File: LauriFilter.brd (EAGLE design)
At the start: 39.3 x 106.5 mm, 27 parts, among them K1 MODE 1, K2 MODE 2

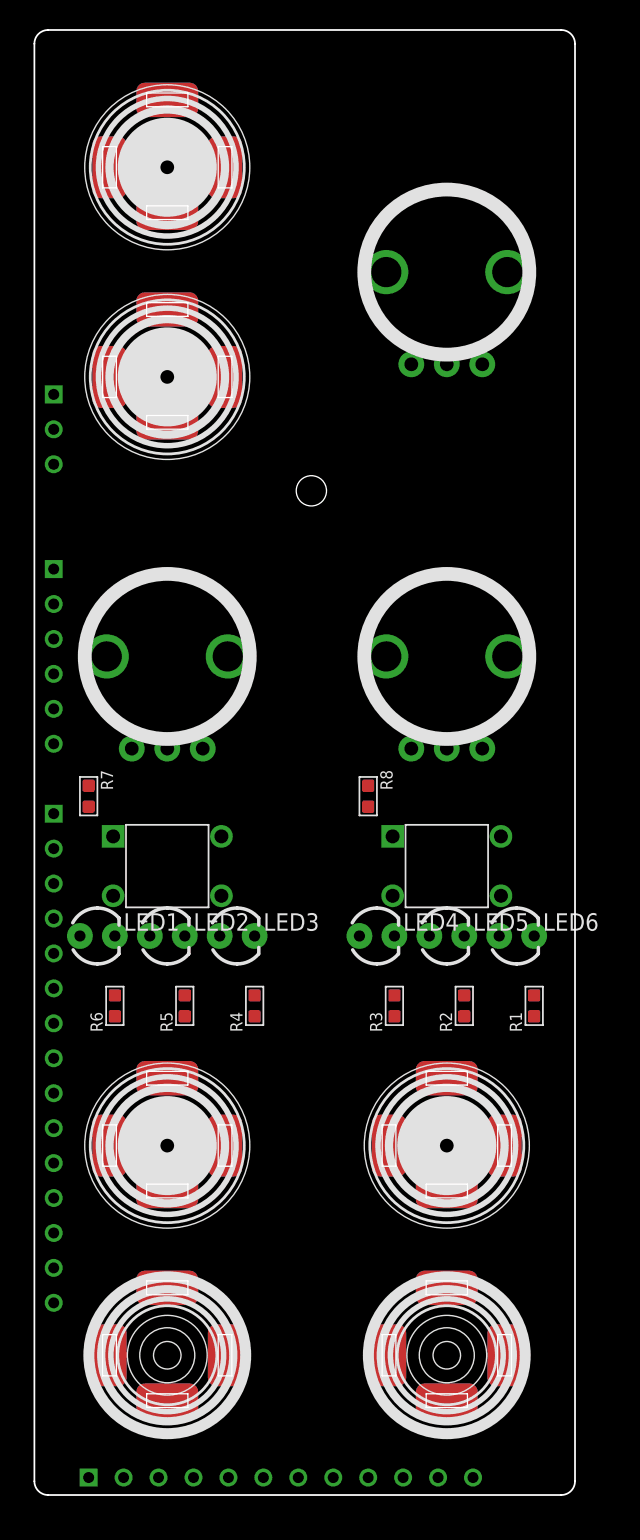
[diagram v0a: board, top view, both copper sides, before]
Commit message: LauriFilter has switches + 595 for leds
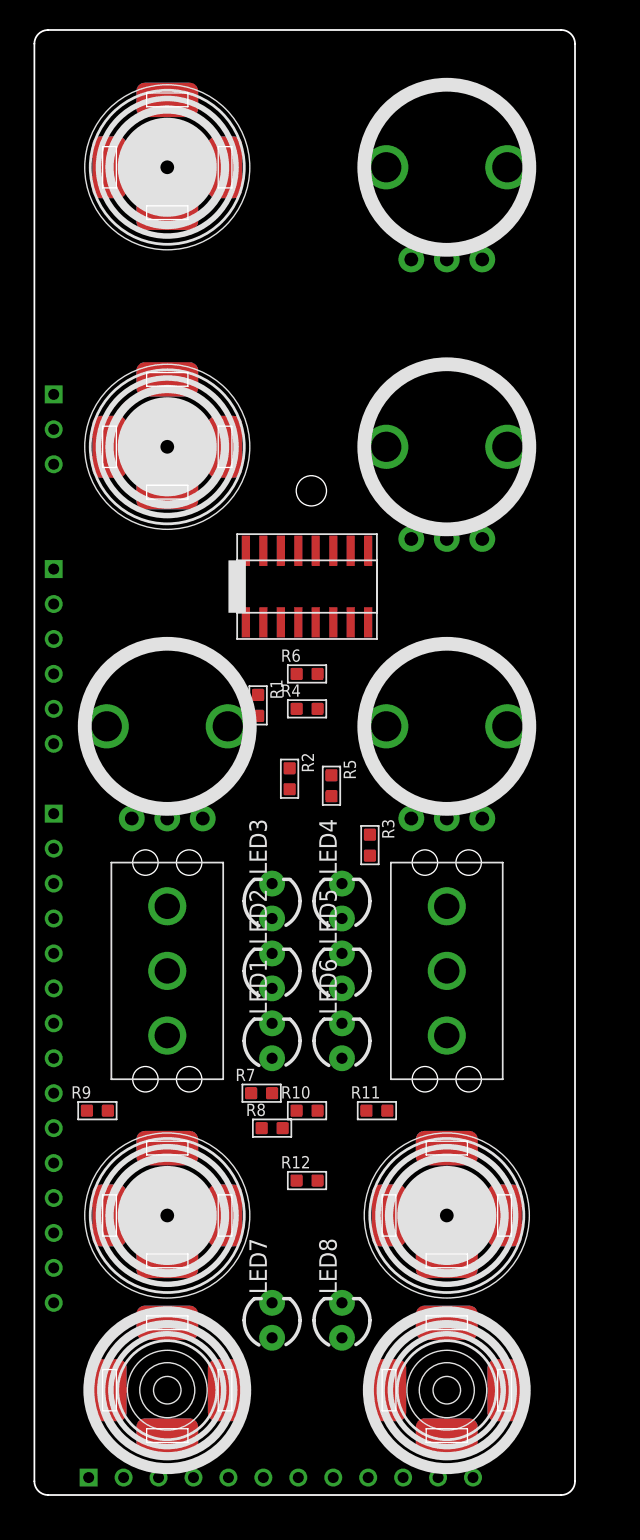
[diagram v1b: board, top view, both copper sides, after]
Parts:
- removed K1: MODE 1, OPL:4P-6.0X6.0X5.0H
- removed K2: MODE 2, OPL:4P-6.0X6.0X5.0H
- added IC2: IC_74HC595-SOIC-16, dp_devices:SOIC-16
- added LED7, LED8: (no value), SparkFun-LED:LED3MM
- added R10, R11, R12, R9: (no value), OPL:R0603
- added U$12, U$13: ONOFFON, EurorackModularParts:MULTICOMP1MS-ONOFFON
- added U$14: CV 2, EurorackModularParts:OG-POTS_ALPS_POT_VERTICAL
- moved R1 29.7 mm to (16.8, 57.4), turned to 270 degrees
- moved R6 27.9 mm to (20.3, 59.7), turned to 0 degrees
- moved R8 25.1 mm to (17.8, 26.7), turned to 0 degrees
- moved R7 25.0 mm to (17.0, 29.2), turned to 0 degrees
- moved R4 21.9 mm to (20.3, 57.1), turned to 0 degrees
- moved R2 20.8 mm to (19.1, 52.1), turned to 270 degrees
- moved R5 19.2 mm to (22.1, 51.6), turned to 270 degrees
- moved LED6 14.8 mm to (22.9, 33.0), turned to 90 degrees
- moved LED1 14.8 mm to (17.8, 33.0), turned to 90 degrees
- moved R3 11.8 mm to (24.9, 47.2), turned to 270 degrees
- moved LED2 8.03 mm to (17.8, 38.1), turned to 90 degrees
- moved LED5 8.03 mm to (22.9, 38.1), turned to 90 degrees
- moved U$9 7.62 mm to (30.5, 96.5)
- moved U$10 5.08 mm to (10.2, 55.9)
- moved U$11 5.08 mm to (30.5, 55.9)
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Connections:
- removed net MODE1: K1.1, K1.2, R7.2, U$1.ADC13
- removed net MODE2: K2.1, K2.2, R8.2, U$1.RX/B16
- removed net N$10: LED3.A, U$1.TX/D7
- removed net N$11: LED4.A, U$1.ADC4
- removed net N$12: LED5.A, U$1.ADC14
- new net LEDB1: IC2.15
- new net LEDB2: IC2.1
- new net LEDB3: IC2.2
- new net LEDB4: IC2.3
- new net LEDB5: IC2.4
- new net LEDB6: IC2.5
- new net LEDB7: IC2.6
- new net LEDB8: IC2.7
- new net LEDCLOCK: IC2.11, U$1.TX/D7
- new net LEDDAT: IC2.14, U$1.ADC4
- new net LEDLATCH: IC2.12, U$1.ADC7
- new net MODE1_A: R7.2, U$1.ADC13, U$12.1
- new net MODE1_B: R8.2, U$1.RX/B16, U$12.3
- new net MODE2_A: R9.2, U$1.TX/B17, U$13.1
- new net MODE2_B: R10.2, U$1.ADC14, U$13.3
- new net N$7: U$14.P$3, U$4.TIP@1, U$4.TIP@2
- net 3.3V: now also IC2.10, R10.1, R9.1
- net GND: now also IC2.13, LED1.A, LED2.A, LED3.A, LED4.A, LED5.A, LED6.A, LED7.A, LED8.A, U$12.2, U$13.2, U$14.P$1; no longer K1.3, K1.4, K2.3, K2.4, R1.1, R2.1, R3.1, R4.1, R5.1, R6.1
- net N$13: now also U$1.ADC6; no longer LED6.A, U$1.TX/B17
- net N$4: no longer U$4.TIP@1, U$4.TIP@2
- net N$8: now also LED8.K, R11.2; no longer LED1.A, U$1.ADC6
- net N$9: now also LED7.K, R12.2; no longer LED2.A, U$1.ADC7

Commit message: Preliminary routing LauriFilter
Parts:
- added C1: 100nF, OPL:C0603
- LED1, LED2, LED3, LED4, LED5, LED6, LED7, LED8: value (none) -> WHITE
- R1, R11, R12, R2, R3, R4, R5, R6: value (none) -> 50
- R10, R7, R8, R9: value (none) -> 10k
- moved IC2 41.9 mm to (20.3, 24.1), flipped to the bottom, turned to 270 degrees
- moved R6 28.0 mm to (14.0, 32.4), flipped to the bottom, turned to 90 degrees
- moved R1 26.9 mm to (26.7, 32.4), flipped to the bottom, turned to 90 degrees
- moved R8 22.5 mm to (33.7, 42.5), flipped to the bottom, turned to 90 degrees
- moved R10 19.8 mm to (6.99, 42.5), flipped to the bottom, turned to 90 degrees
- moved R7 17.2 mm to (33.7, 33.7), flipped to the bottom, turned to 270 degrees
- moved R2 16.5 mm to (26.7, 37.5), flipped to the bottom, turned to 90 degrees
- moved R5 16.3 mm to (14.0, 37.5), flipped to the bottom, turned to 90 degrees
- moved R4 15.9 mm to (14.0, 42.5), flipped to the bottom, turned to 90 degrees
- moved R11 11.1 mm to (22.9, 17.1), flipped to the bottom, turned to 270 degrees
- moved R12 6.25 mm to (17.8, 17.1), flipped to the bottom, turned to 270 degrees
- moved R9 6.02 mm to (6.99, 33.7), flipped to the bottom, turned to 270 degrees
- moved R3 5.02 mm to (26.7, 42.5), flipped to the bottom, turned to 90 degrees
- turned LED1 to 180 degrees
- turned LED2 to 180 degrees
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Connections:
- removed net N$13: U$1.ADC6
- net 3.3V: now also C1.2, IC2.16, U$1.3.3V
- net GND: now also C1.1, IC2.8
- net LEDB1: now also R6.1
- net LEDB2: now also R5.1
- net LEDB3: now also R4.1
- net LEDB4: now also R3.1
- net LEDB5: now also R2.1
- net LEDB6: now also R1.1
- net LEDB7: now also R12.1
- net LEDB8: now also R11.1
- net N$4: now also U$14.P$2
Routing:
- net GND: track 0.00 -> 390.1 mm, vias 0 -> 1
- net 3.3V: track 0.00 -> 154.5 mm
- net CUTOFF: track 0.00 -> 68.3 mm
- net MODE1_B: track 0.00 -> 52.5 mm
- net MODE1_A: track 0.00 -> 38.6 mm
- net N$2: track 0.00 -> 37.9 mm, vias 0 -> 1
- net DRIVE: track 0.00 -> 36.3 mm, vias 0 -> 1
- net N$7: track 0.00 -> 32.0 mm, vias 0 -> 1
- net N$3: track 0.00 -> 31.9 mm, vias 0 -> 1
- net N$1: track 0.00 -> 31.9 mm, vias 0 -> 1
- net N$4: track 0.00 -> 30.9 mm
- net MODE2_B: track 0.00 -> 23.0 mm
- net LEDLATCH: track 0.00 -> 22.5 mm, vias 0 -> 1
- net N$5: track 0.00 -> 20.8 mm, vias 0 -> 1
- net LEDB3: track 0.00 -> 20.3 mm, vias 0 -> 2
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
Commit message: Many many changes after crosschecking by Lauri
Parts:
- added R13: 100k, OPL:R0603
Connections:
- new net N$10: R13.2, U$14.P$3
- net N$7: now also R13.1; no longer U$14.P$3
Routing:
- net GND: track 390.1 -> 0.00 mm, vias 1 -> 0
- net 3.3V: track 154.5 -> 0.00 mm
- net CUTOFF: track 68.3 -> 0.00 mm
- net MODE1_B: track 52.5 -> 0.00 mm
- net MODE1_A: track 38.6 -> 0.00 mm
- net N$2: track 37.9 -> 0.00 mm, vias 1 -> 0
- net DRIVE: track 36.3 -> 0.00 mm, vias 1 -> 0
- net N$7: track 32.0 -> 0.00 mm, vias 1 -> 0
- net N$3: track 31.9 -> 0.00 mm, vias 1 -> 0
- net N$1: track 31.9 -> 0.00 mm, vias 1 -> 0
- net N$4: track 30.9 -> 0.00 mm
- net MODE2_B: track 23.0 -> 0.00 mm
- net LEDLATCH: track 22.5 -> 0.00 mm, vias 1 -> 0
- net N$5: track 20.8 -> 0.00 mm, vias 1 -> 0
- net LEDB3: track 20.3 -> 0.00 mm, vias 2 -> 0
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
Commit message: pre order fixes
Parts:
- added D1: BAS70-04, diode:SOT23
- added JP1: M02PTH, SparkFun-Connectors:1X02
- added R14, R15: 300, OPL:C0805
- added R16: 300, OPL:R0603
- moved U$10 20.3 mm to (30.5, 55.9)
- moved U$11 20.3 mm to (10.2, 55.9)
- turned LED7 to 180 degrees
- turned LED8 to 180 degrees
- turned R7 to 90 degrees
- turned R8 to 270 degrees
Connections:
- new net N$11: R14.1, U$1.OUT_L
- new net N$12: R15.1, U$1.OUT_R
- new net N$13: D1.3, R16.2, U$1.OUT_DAC
- new net N$20: JP1.2, R16.1
- net 3.3V: now also D1.2
- net GND: now also D1.1, JP1.1
- net N$5: now also R14.2; no longer U$1.OUT_L
- net N$6: now also R15.2; no longer U$1.OUT_R
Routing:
- net 3.3V: track 0.00 -> 157.5 mm, vias 0 -> 3
- net CUTOFF: track 0.00 -> 69.7 mm
- net GND: track 0.00 -> 59.8 mm, vias 0 -> 13
- net N$2: track 0.00 -> 57.8 mm, vias 0 -> 1
- net MODE1_B: track 0.00 -> 39.4 mm, vias 0 -> 2
- net MODE1_A: track 0.00 -> 39.4 mm, vias 0 -> 4
- net RESONANCE: track 0.00 -> 38.2 mm
- net N$3: track 0.00 -> 33.1 mm, vias 0 -> 1
- net N$4: track 0.00 -> 30.9 mm
- net N$1: track 0.00 -> 30.7 mm, vias 0 -> 1
- net N$13: track 0.00 -> 30.6 mm
- net LEDCLOCK: track 0.00 -> 27.9 mm
- net LEDLATCH: track 0.00 -> 24.9 mm
- net MODE2_B: track 0.00 -> 24.5 mm, vias 0 -> 2
- net LEDB3: track 0.00 -> 23.5 mm, vias 0 -> 4
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- added copper zone on layer 1, net GND
